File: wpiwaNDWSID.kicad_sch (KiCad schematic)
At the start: 14 parts, among them J2 Conn_01x03, J3 Conn_01x03, J4 Conn_01x03, J5 Conn_01x02, J6 Conn_01x03, U3 AP63205WU, U4 AP7363-33D-13

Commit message: final design
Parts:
- removed C5: 2200uF, Capacitor_THT:CP_Radial_D8.0mm_P3.80mm, symbol Device:C_Polarized
- removed J2, J3, J4, J6: Conn_01x03, Connector_Wire:SolderWire-1.5sqmm_1x03_P7.8mm_D1.7mm_OD3.9mm, symbol Connector_Generic:Conn_01x03
- added J2: Conn_01x04, Connector_Wire:SolderWire-1.5sqmm_1x04_P7.8mm_D1.7mm_OD3.9mm, symbol Connector_Generic:Conn_01x04
- J5: footprint Connector_Wire:SolderWire-2sqmm_1x02_P7.8mm_D2mm_OD3.9mm -> Connector_Wire:SolderWire-1.5sqmm_1x02_P7.8mm_D1.7mm_OD3.9mm
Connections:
- net LED Driver/LED1_OUT: now also J2.1 (Pin_1)
- net LED Driver/LED2_OUT: now also J2.2 (Pin_2)
- net LED Driver/LED3_OUT: now also J2.3 (Pin_3)
- net LED Driver/LED4_OUT: now also J2.4 (Pin_4)
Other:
- moved on the sheet: C4

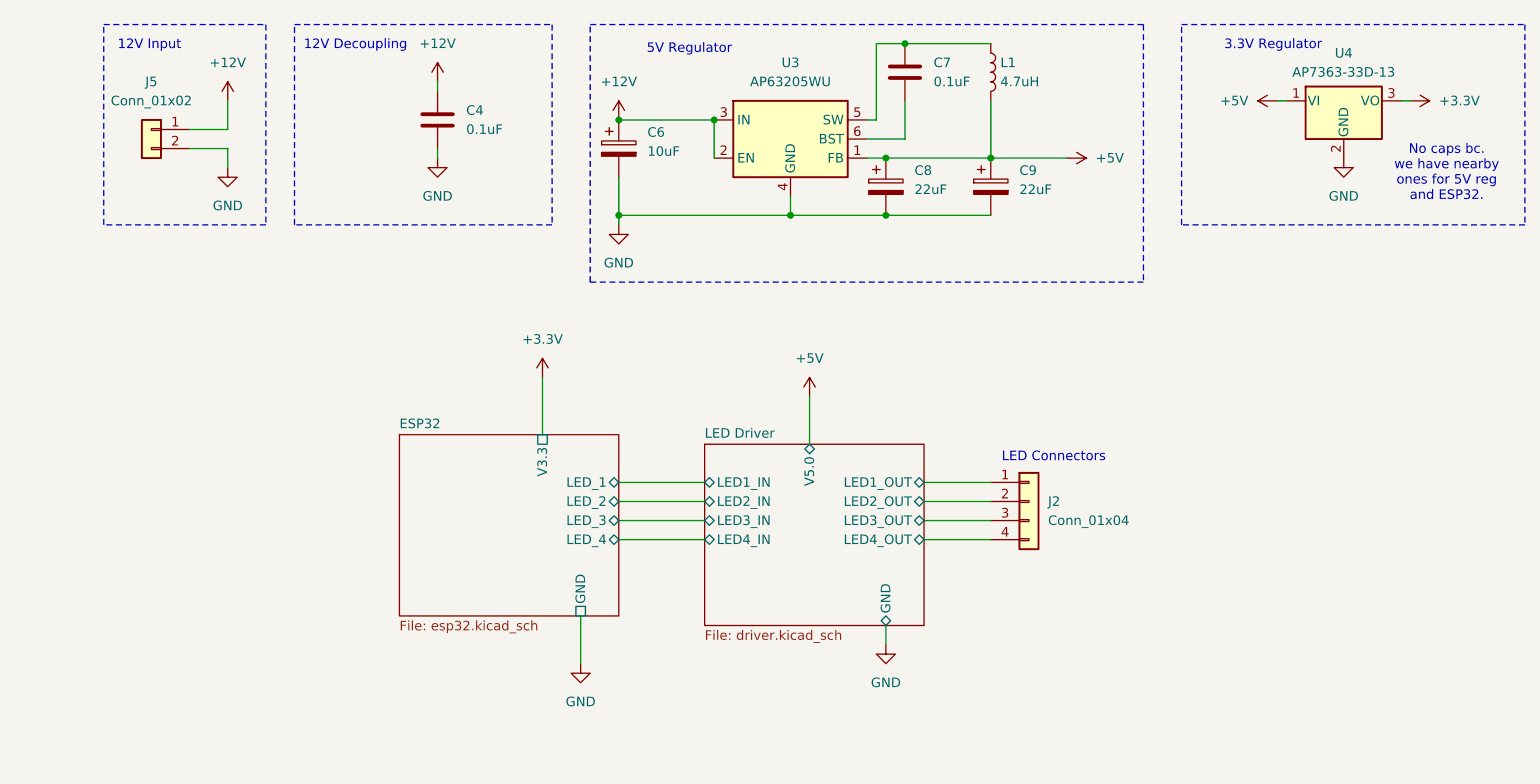
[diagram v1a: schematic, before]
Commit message: all one layer added usb
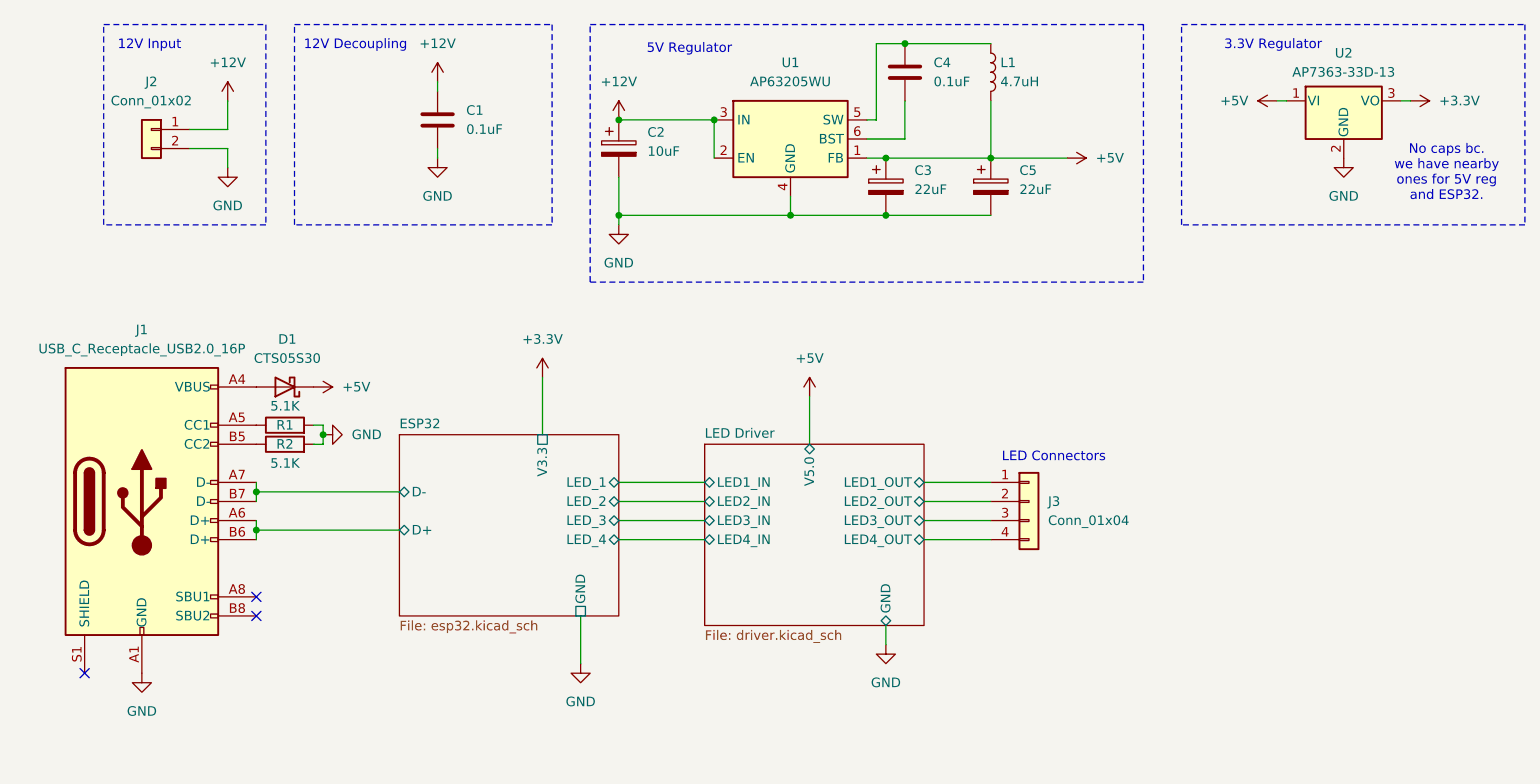
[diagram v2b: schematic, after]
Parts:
- added D1: CTS05S30, Diode_SMD:D_0805_2012Metric, symbol Diode:B220
- added J1: USB_C_Receptacle_USB2.0_16P, Connector_USB:USB_C_Receptacle_GCT_USB4105-xx-A_16P_TopMnt_Horizontal, symbol Connector:USB_C_Receptacle_USB2.0_16P
- added R1, R2: 5.1K, Resistor_SMD:R_0402_1005Metric, symbol Device:R
- C1: renamed from C4; footprint Capacitor_SMD:C_0402_1005Metric_Pad0.74x0.62mm_HandSolder -> Capacitor_SMD:C_0402_1005Metric
- C4: renamed from C7; footprint Capacitor_SMD:C_0402_1005Metric_Pad0.74x0.62mm_HandSolder -> Capacitor_SMD:C_0402_1005Metric
- renumbered C6 to C2, C8 to C3, C9 to C5, J5 to J2, J2 to J3, U3 to U1, U4 to U2
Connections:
- net +5V: now also D1.1 (K)
- net GND: now also J1.A1 (GND), J1.A12 (GND), J1.B1 (GND), J1.B12 (GND), R1.2, R2.2
- new net: D1.2 (A), J1.A4 (VBUS), J1.A9 (VBUS), J1.B4 (VBUS), J1.B9 (VBUS)
- new net: J1.A5 (CC1), R1.1
- new net: J1.B5 (CC2), R2.1
- new net ESP32/D+: J1.A6 (D+), J1.B6 (D+)
- new net ESP32/D-: J1.A7 (D-), J1.B7 (D-)
- no-connect marks 0 -> 3
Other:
- sheet ESP32 ports: added D+, D-; removed none

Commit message: rev 2
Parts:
- removed C1, C4: 0.1uF, Capacitor_SMD:C_0402_1005Metric, symbol Device:C
- removed C2: 10uF, Capacitor_THT:CP_Radial_D4.0mm_P2.00mm, symbol Device:C_Polarized
- removed C3, C5: 22uF, Capacitor_THT:CP_Radial_D4.0mm_P2.00mm, symbol Device:C_Polarized
- removed L1: 4.7uH, Inductor_SMD:L_0603_1608Metric_Pad1.05x0.95mm_HandSolder, symbol Device:L
- removed U1: AP63205WU, Package_TO_SOT_SMD:TSOT-23-6_HandSoldering, symbol Regulator_Switching:AP63205WU
- added C1: 22uF, Capacitor_THT:CP_Radial_D4.0mm_P2.00mm, symbol Device:C_Polarized
- added D2: CTS05S30, Diode_SMD:D_0402_1005Metric_Pad0.77x0.64mm_HandSolder, symbol Diode:B220
- added J4: Conn_01x03, Connector_Wire:SolderWire-0.75sqmm_1x03_P4.8mm_D1.25mm_OD2.3mm, symbol Connector_Generic:Conn_01x03
- D1: footprint Diode_SMD:D_0805_2012Metric -> Diode_SMD:D_0402_1005Metric_Pad0.77x0.64mm_HandSolder
- J2: footprint Connector_Wire:SolderWire-1.5sqmm_1x02_P7.8mm_D1.7mm_OD3.9mm -> Connector_Wire:SolderWire-0.75sqmm_1x02_P4.8mm_D1.25mm_OD2.3mm
- J3: footprint Connector_Wire:SolderWire-1.5sqmm_1x04_P7.8mm_D1.7mm_OD3.9mm -> Connector_Wire:SolderWire-0.75sqmm_1x04_P4.8mm_D1.25mm_OD2.3mm
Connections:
- net +3.3V: now also J4.1 (Pin_1)
- net +5V: now also C1.1, D2.1 (K)
- net GND: now also C1.2, J4.3 (Pin_3)
- net +12V: no longer names the net of J2.1 (Pin_1)
- net +12V: now also D2.2 (A)
- new net ESP32/RELAY: J4.2 (Pin_2)
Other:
- sheet ESP32 ports: added RELAY; removed none
- note added: "5V Input"
- note removed: "12V Decoupling"
- note removed: "12V Input"
- note removed: "5V Regulator"
- note removed: "No caps bc. we have nearby ones for 5V reg and ESP32."
- moved on the sheet: U2
